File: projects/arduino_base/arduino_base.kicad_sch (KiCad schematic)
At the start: 40 parts, among them Q1 MMBT2222A, U1 FT231, U2 ATMEGA328P, U3 RS3112-4.096X, X1 USB C, X2 Programming, X3 16MHz

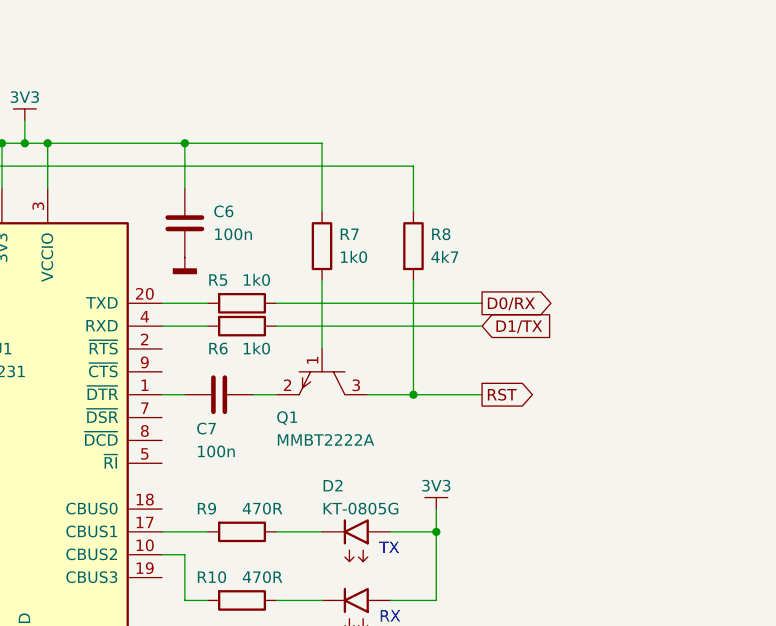
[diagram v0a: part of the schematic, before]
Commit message: fix reset circuitry
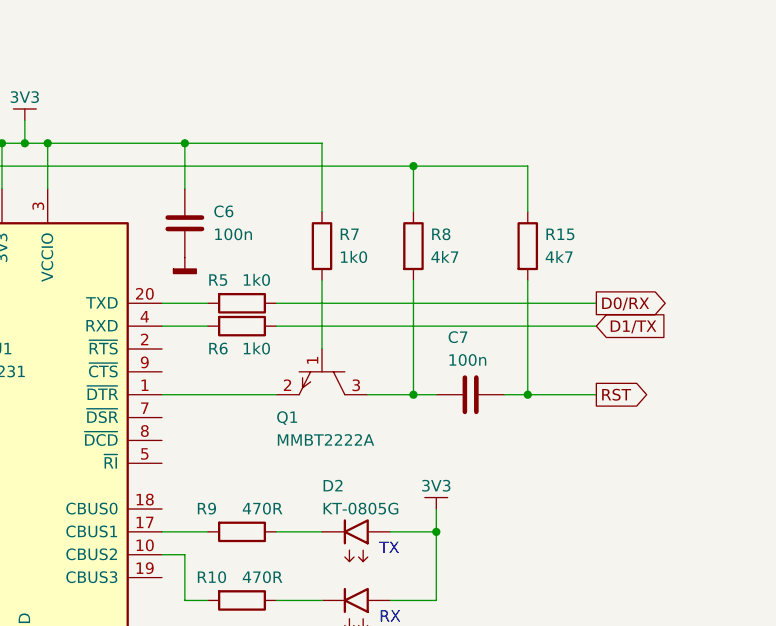
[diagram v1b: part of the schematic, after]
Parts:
- added R15: 4k7, lily_footprints:res_0805, symbol lily_symbols:res_4k7_1%_125mW_0805
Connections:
- net 5V: now also R15.1
- net RST: now also C7.1, R15.2; no longer Q1.3, R8.2
- net at U1.1 (~{DTR}): now also Q1.2; no longer C7.2
- new net: C7.2, Q1.3, R8.2
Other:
- moved on the sheet: C7

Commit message: updated project
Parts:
- C1, C2: JLCPCB_ID C24659 -> NO_ID; JLCPCB_STATUS Extended -> (none); Manufacturer Guangdong Fenghua Advanced Tech -> TODO; Manufacturer_ID 0805CG470J500NT -> TODO
- C10, C13, C14, C4, C6, C7: JLCPCB_ID C49678 -> NO_ID; JLCPCB_STATUS Basic -> (none); Manufacturer YAGEO -> TODO; Manufacturer_ID CC0805KRX7R9BB104 -> TODO
- C11, C12: JLCPCB_ID C28323 -> NO_ID; JLCPCB_STATUS Basic -> (none); Manufacturer Samsung Electro-Mechanics -> TODO; Manufacturer_ID CL21B105KBFNNNE -> TODO
- C3: JLCPCB_ID C1710 -> NO_ID; JLCPCB_STATUS Basic -> (none); Manufacturer Samsung Electro-Mechanics -> TODO; Manufacturer_ID CL21B103KBANNNC -> TODO
- C5: JLCPCB_ID C1779 -> NO_ID; JLCPCB_STATUS Basic -> (none); Manufacturer Samsung Electro-Mechanics -> TODO; Manufacturer_ID CL21A475KAQNNNE -> TODO
- C8, C9: JLCPCB_ID C1804 -> NO_ID; JLCPCB_STATUS Basic -> (none); Manufacturer Samsung Electro-Mechanics -> TODO; Manufacturer_ID CL21C220JBANNNC -> TODO
- D1: JLCPCB_ID C85364 -> NO_ID; JLCPCB_STATUS Extended Preferred -> (none); Lily_ID 1911-10004 -> NO_ID; Manufacturer ProTek Devices -> TODO; Manufacturer_ID SRV05-4-P-T7 -> TODO
- D2, D3: JLCPCB_ID C2297 -> NO_ID; JLCPCB_STATUS Basic -> (none); Manufacturer Hubei KENTO Elec -> TODO; Manufacturer_ID KT-0805G -> TODO
- L1, L2: JLCPCB_ID C21286 -> NO_ID; JLCPCB_STATUS Extended -> (none); Manufacturer Guangdong Fenghua Advanced Tech -> TODO; Manufacturer_ID CBW201209U601T -> TODO
- Q1: value MMBT2222A -> MMBT2222AL
- R1, R2: JLCPCB_ID C27834 -> NO_ID; JLCPCB_STATUS Basic -> (none); Manufacturer Uniroyal Electronics -> TODO; Manufacturer_ID 0805W8F5101T5E -> TODO
- R10, R9: JLCPCB_ID C17710 -> NO_ID; JLCPCB_STATUS Basic -> (none); Manufacturer Uniroyal Electronics -> TODO; Manufacturer_ID 0805W8F4700T5E -> TODO
- R11, R12, R13, R14: JLCPCB_ID C17557 -> NO_ID; JLCPCB_STATUS Basic -> (none); Manufacturer Uniroyal Electronics -> TODO; Manufacturer_ID 0805W8F2200T5E -> TODO
- R15, R8: JLCPCB_ID C17673 -> NO_ID; JLCPCB_STATUS Basic -> (none); Manufacturer Uniroyal Electronics -> TODO; Manufacturer_ID 0805W8F4701T5E -> TODO
- R3, R4: JLCPCB_ID C17594 -> NO_ID; JLCPCB_STATUS Extended preferred -> (none); Manufacturer Uniroyal Electronics -> TODO; Manufacturer_ID 0805W8F270JT5E -> TODO
- R5, R6, R7: JLCPCB_ID C17513 -> NO_ID; JLCPCB_STATUS Basic -> (none); Manufacturer Uniroyal Electronics -> TODO; Manufacturer_ID 0805W8F1001T5E -> TODO
- U1: JLCPCB_ID C132160 -> NO_ID; JLCPCB_STATUS Extended -> (none); Lily_ID 1914-10008 -> NO_ID; Manufacturer FTDI -> TODO; Manufacturer_ID FT231XS-R -> TODO
- U2: JLCPCB_ID C14877 -> NO_ID; JLCPCB_STATUS Extended -> (none); Manufacturer Microchip -> TODO; Manufacturer_ID ATMEGA328P-AU -> TODO
- U3: JLCPCB_ID C19269198 -> NO_ID; JLCPCB_STATUS Extended -> (none); Manufacturer Jiangsu RUNIC Tech -> TODO; Manufacturer_ID RS3112-4.096XSF3 -> TODO
- X1: JLCPCB_ID C2765186 -> NO_ID; JLCPCB_STATUS Extended -> (none); Manufacturer Shou Han -> TODO; Manufacturer_ID TYPE-C 16PIN 2MD(073) -> TODO
- X2: JLCPCB_ID C492420 -> NO_ID; JLCPCB_STATUS Extended -> (none); Lily_ID 1910-10004 -> NO_ID; Manufacturer XFCN -> TODO; Manufacturer_ID PZ254V-12-6P -> TODO
- X3: JLCPCB_ID C156247 -> NO_ID; JLCPCB_STATUS Extended -> (none); Lily_ID 1917-10001 -> NO_ID; Manufacturer NDK -> TODO; Manufacturer_ID NX3225GA-16MHZ-STD-CRG-2 -> TODO

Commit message: updated project
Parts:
- removed C13: 100n, lily_footprints:cap_0805, symbol lily_symbols:cap_100n_50V_10%_X7R_0805
- C1, C2: JLCPCB_ID NO_ID -> C107118; Manufacturer TODO -> YAGEO; Manufacturer_ID TODO -> CC0805JRNPO9BN470
- C10, C14, C4, C6, C7: JLCPCB_ID NO_ID -> C49678; Manufacturer TODO -> YAGEO; Manufacturer_ID TODO -> CC0805KRX7R9BB104
- C11, C12: JLCPCB_ID NO_ID -> C28323; Manufacturer TODO -> Samsung Electro-Mechanics; Manufacturer_ID TODO -> CL21B105KBFNNNE
- C3: JLCPCB_ID NO_ID -> C83170; Manufacturer TODO -> YAGEO; Manufacturer_ID TODO -> CC0805KRX7R9BB103
- C5: JLCPCB_ID NO_ID -> C1779; Manufacturer TODO -> Samsung Electro-Mechanics; Manufacturer_ID TODO -> CL21A475KAQNNNE
- C8, C9: JLCPCB_ID NO_ID -> C105623; Manufacturer TODO -> YAGEO; Manufacturer_ID TODO -> CC0805JRNPO9BN220
- D1: JLCPCB_ID NO_ID -> C1975211; Manufacturer TODO -> Littelfuse; Manufacturer_ID TODO -> SRV05-4HTG-D
- D2, D3: value KT-0805G -> KP-2012CGCK; symbol lily_symbols:dio_led_green_KT-0805G_0805 -> lily_symbols:dio_led_green_KP-2012CGCK_0805; JLCPCB_ID NO_ID -> C598271; Manufacturer TODO -> Kingbright; Manufacturer_ID TODO -> KP-2012CGCK
- L1, L2: value 600R/0R25 -> 600R/0R1; symbol lily_symbols:ind_bead_600R@100MHz_1A5_0R25_0805 -> lily_symbols:ind_bead_600R@100MHz_2A_0R1_0805; JLCPCB_ID NO_ID -> C21519; Manufacturer TODO -> TDK; Manufacturer_ID TODO -> MPZ2012S601AT000
- Q1: symbol lily_symbols:bjt_npn_MMBT2222A_sot23 -> lily_symbols:bjt_npn_MMBT2222AL_sot23; JLCPCB_ID C8512 -> C82460; JLCPCB_STATUS Basic -> (none); Manufacturer Jiangsu Changjing Electronics Technology -> onsemi; Manufacturer_ID MMBT2222A -> MMBT2222ALT1G
- R1, R2: JLCPCB_ID NO_ID -> C84375; Manufacturer TODO -> YAGEO; Manufacturer_ID TODO -> RC0805FR-075K1L
- R10, R9: JLCPCB_ID NO_ID -> C114564; Manufacturer TODO -> YAGEO; Manufacturer_ID TODO -> RC0805FR-07470RL
- R11, R12, R13, R14: JLCPCB_ID NO_ID -> C114519; Manufacturer TODO -> YAGEO; Manufacturer_ID TODO -> RC0805FR-07220RL
- R15, R8: JLCPCB_ID NO_ID -> C60816; Manufacturer TODO -> YAGEO; Manufacturer_ID TODO -> RC0805FR-074K7L
- R3, R4: JLCPCB_ID NO_ID -> C163408; Manufacturer TODO -> YAGEO; Manufacturer_ID TODO -> RC0805FR-0727RL
- R5, R6, R7: JLCPCB_ID NO_ID -> C95781; Manufacturer TODO -> YAGEO; Manufacturer_ID TODO -> RC0805FR-071KL
- U1: value FT231 -> FT231XS; symbol lily_symbols:ic_usb_to_serial_FT231_ssop20 -> lily_symbols:ic_usb_to_serial_FT231XS_ssop20; JLCPCB_ID NO_ID -> C132160; Manufacturer TODO -> FTDI; Manufacturer_ID TODO -> FT231XS
- U2: value ATMEGA328P -> ATMEGA328PB; symbol lily_symbols:ic_micro_controller_ATMEGA328P_tqfp32 -> lily_symbols:ic_micro_controller_ATMEGA328PB_tqfp32; JLCPCB_ID NO_ID -> C132230; Manufacturer TODO -> Microchip Tech; Manufacturer_ID TODO -> ATMEGA328PB-AU
- U3: value RS3112-4.096X -> REF3040; symbol lily_symbols:ic_volt_reference_RS3112-4.096X_sot23 -> lily_symbols:ic_volt_reference_REF3040_4.096V_sot23; JLCPCB_ID NO_ID -> C19415; Manufacturer TODO -> Texas Instruments; Manufacturer_ID TODO -> REF3040AIDBZR
- X1: value USB C -> con_usb_c_receptacle_16p; JLCPCB_ID NO_ID -> C2765186; Manufacturer TODO -> SHOU HAN; Manufacturer_ID TODO -> TYPE-C 16PIN 2MD(073)
- X2: value Programming -> ISP; Manufacturer TODO -> Multicomp; Manufacturer_ID TODO -> 2213S-06G
- X3: symbol lily_symbols:crystal_16MHz_20ppm_8pF_3225 -> lily_symbols:crystal_16MHz_12pF_10ppm_20ppm_3225; JLCPCB_ID NO_ID -> C89371; Manufacturer TODO -> Seiko Epson; Manufacturer_ID TODO -> X1E0000210119
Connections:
- net GND: no longer U2.3 (GND)
- net 3V3 renamed +3V3
- net 5V renamed +5V
- net +5V: no longer U2.6 (VCC)
